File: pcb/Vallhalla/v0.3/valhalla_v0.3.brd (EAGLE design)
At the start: 92.7 x 55.5 mm, 17 parts, among them J1 POWER_JACKPTH, U1 LM317, U2 TLC5940-NT

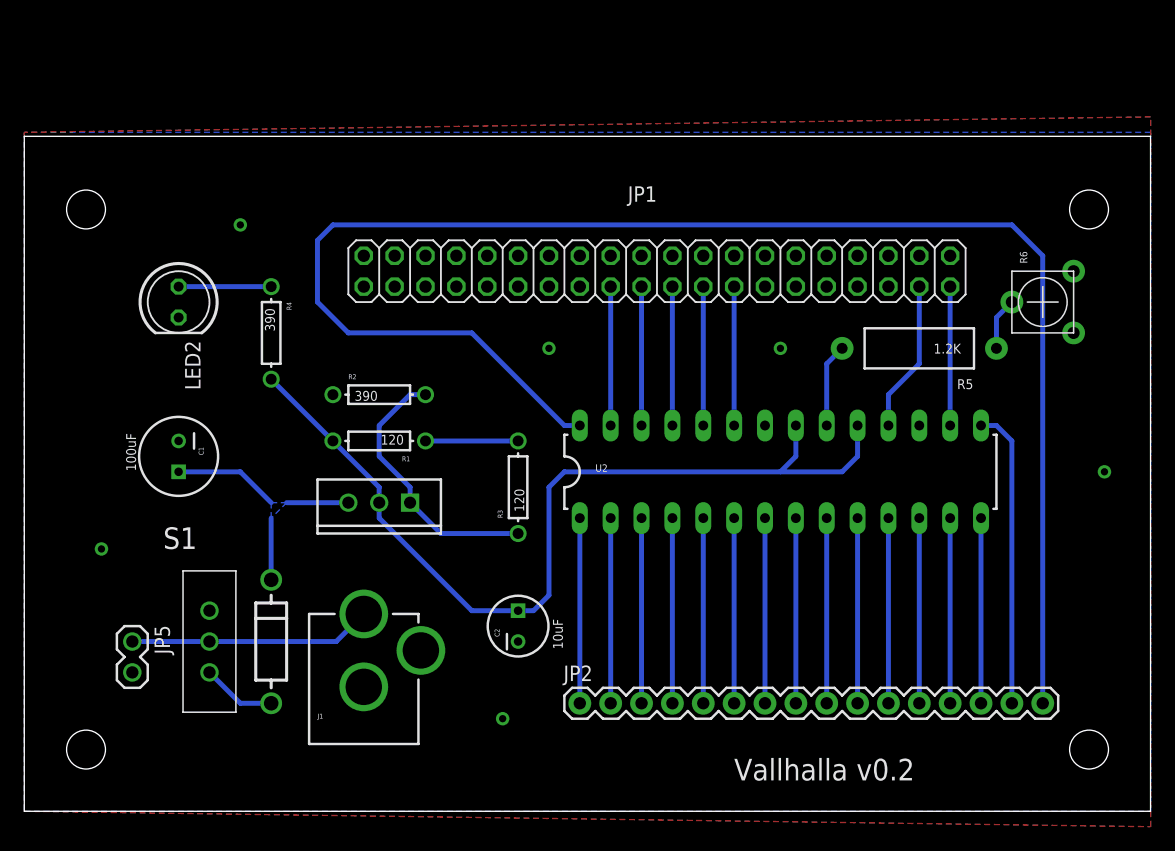
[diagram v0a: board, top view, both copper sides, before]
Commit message: Version 3
Added ULN2003
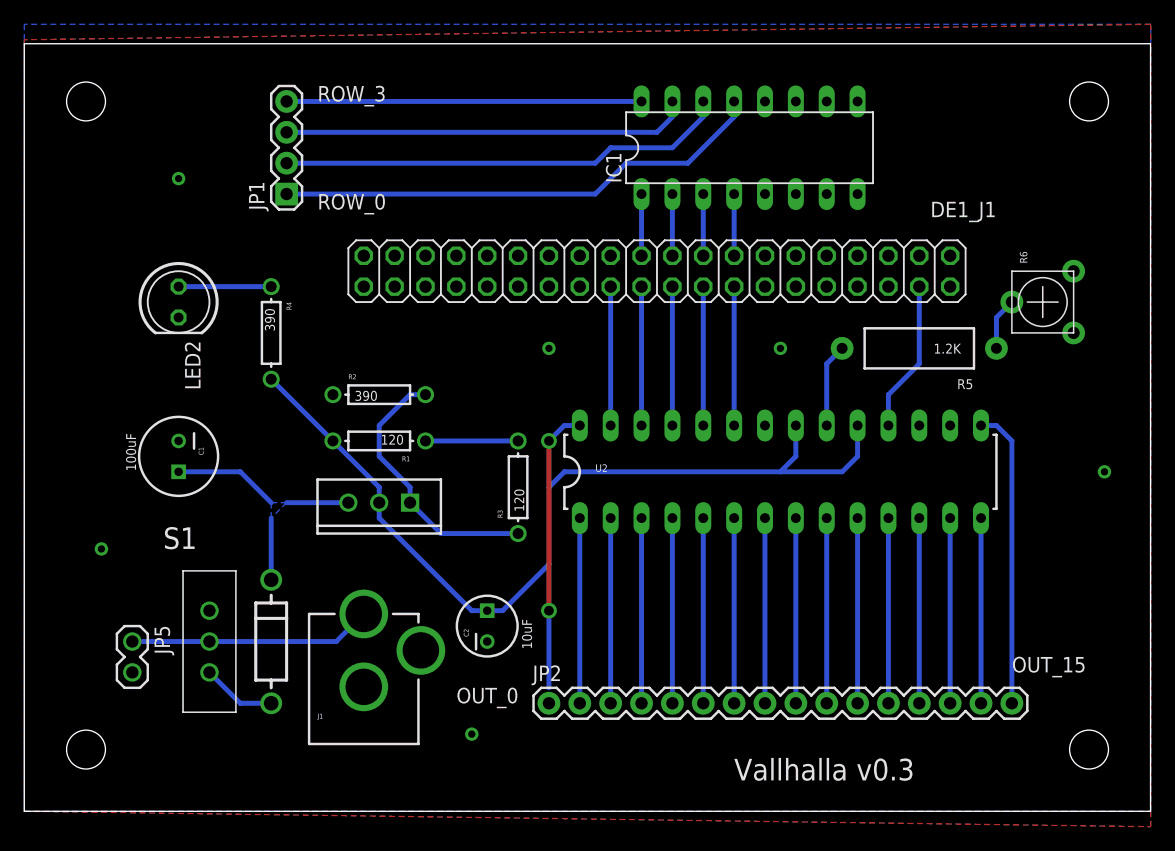
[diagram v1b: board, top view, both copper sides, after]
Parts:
- added DE1_J1: (no value), connectors:2X20
- added IC1: ULN2003AN, uln-udn:DIL16
- JP1: device adafruit:2X20 -> SparkFun-Connectors:1X04
- moved JP1 31.1 mm to (16.5, 45.7), turned to 90 degrees
- moved C2 2.54 mm to (33.0, 10.2)
- moved JP2 2.54 mm to (38.1, 3.81)
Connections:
- new net N$21: DE1_J1.15, IC1.4
- new net N$23: DE1_J1.17, IC1.3
- new net N$25: DE1_J1.19, IC1.2
- new net N$26: DE1_J1.21, IC1.1
- new net N$27: IC1.13, JP1.1
- new net N$28: IC1.14, JP1.2
- new net N$29: IC1.15, JP1.3
- new net N$30: IC1.16, JP1.4
- new net VCC33: DE1_J1.29
- new net VCC5: DE1_J1.11
- net BLANK: now also DE1_J1.16; no longer JP1.16
- net GND: now also DE1_J1.12, DE1_J1.30, IC1.8; no longer JP1.12, JP1.30
- net GSCLK: now also DE1_J1.4; no longer JP1.4
- net N$1: now also JP2.16, U2.15; no longer JP2.1, U2.1
- net N$10: now also JP2.11, U2.10; no longer JP2.6, U2.6
- net N$11: now also JP2.10, U2.9; no longer JP2.7, U2.7
- net N$12: now also JP2.9; no longer JP2.8
- net N$13: now also JP2.8, U2.7; no longer JP2.9, U2.9
- net N$14: now also JP2.7, U2.6; no longer JP2.10, U2.10
- net N$15: now also JP2.6, U2.5; no longer JP2.11, U2.11
- net N$16: now also JP2.5, U2.4; no longer JP2.12, U2.12
- net N$17: now also JP2.4, U2.3; no longer JP2.13, U2.13
- net N$18: now also JP2.3, U2.2; no longer JP2.14, U2.14
- net N$19: now also JP2.2, U2.1; no longer JP2.15, U2.15
- net N$20: now also JP2.1; no longer JP2.16
- net N$4: now also JP2.15, U2.14; no longer JP2.2, U2.2
- net N$6: now also JP2.14, U2.13; no longer JP2.3, U2.3
- net N$7: now also JP2.13, U2.12; no longer JP2.4, U2.4
- net N$9: now also JP2.12, U2.11; no longer JP2.5, U2.5
- net SCLK: now also DE1_J1.20; no longer JP1.20
- net SIN: now also DE1_J1.22; no longer JP1.22
- net VPRG: now also DE1_J1.24; no longer JP1.24
- net XERR: now also DE1_J1.2; no longer JP1.2
- net XLAT: now also DE1_J1.18; no longer JP1.18
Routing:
- net N$20: track 129.0 -> 23.4 mm, vias 0 -> 2
- net N$27: track 0.00 -> 40.7 mm
- net N$28: track 0.00 -> 37.1 mm
- net N$29: track 0.00 -> 33.5 mm
- net N$30: track 0.00 -> 29.2 mm
- net XERR: track 11.4 -> 0.00 mm
- net N$19: track 24.7 -> 15.2 mm
- net N$1: track 15.2 -> 24.7 mm
- net N$26: track 0.00 -> 5.08 mm
- net N$25: track 0.00 -> 5.08 mm
- net N$23: track 0.00 -> 5.08 mm
- net N$21: track 0.00 -> 5.08 mm
- net VCC: track 75.0 -> 73.5 mm
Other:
- board size 92.7 x 55.5 mm -> 92.7 x 63.2 mm
- board text added: "OUT_0"
- board text added: "OUT_15"
- board text added: "ROW_0"
- board text added: "ROW_3"
- board text added: "Vallhalla v0.3"
- board text added: "Vallhalla v0.5"
- board text removed: "Vallhalla v0.2"
